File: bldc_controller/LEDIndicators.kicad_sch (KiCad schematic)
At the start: 4 parts

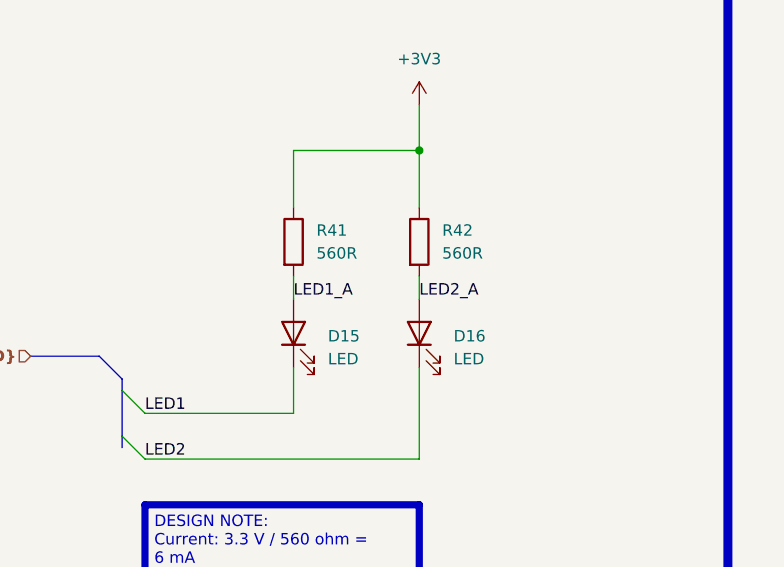
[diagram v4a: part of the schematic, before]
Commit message: routed all signals. TODO: redo all power polygons and ensure good return paths/reference. Added 3d models
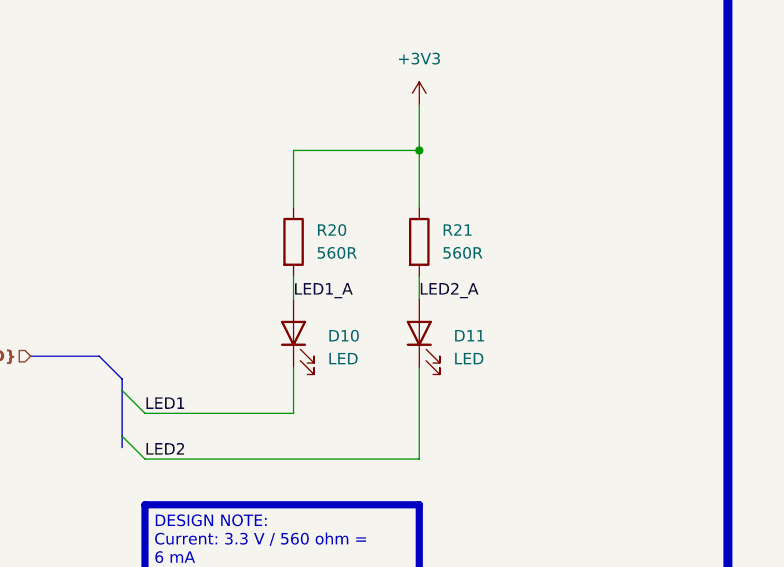
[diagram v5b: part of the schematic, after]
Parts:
- renumbered D15 to D10, D16 to D11, R41 to R20, R42 to R21
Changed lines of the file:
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@@
   (symbol (lib_id "Device:R") (at 162.56 78.74 0) (unit 1)
     (in_bom yes) (on_board yes) (dnp no) (fields_autoplaced)
-    (property "Reference" "R42" (at 165.1 77.47 0)
+    (property "Reference" "R21" (at 165.1 77.47 0)
       (effects (font (size 1.27 1.27)) (justify left))
     )
@@
       (project "bldc_controller"
         (path "/0650c7a8-acba-429c-9f8e-eec0baf0bc1c/fede4c36-00cc-4d3d-b71c-5243ba232202/37954a46-d14f-4062-b94e-09ed11854078"
-          (reference "R42") (unit 1)
+          (reference "R21") (unit 1)
         )
       )
@@
   (symbol (lib_id "Device:R") (at 148.59 78.74 0) (unit 1)
     (in_bom yes) (on_board yes) (dnp no) (fields_autoplaced)
-    (property "Reference" "R41" (at 151.13 77.47 0)
+    (property "Reference" "R20" (at 151.13 77.47 0)
       (effects (font (size 1.27 1.27)) (justify left))
     )
@@
       (project "bldc_controller"
         (path "/0650c7a8-acba-429c-9f8e-eec0baf0bc1c/fede4c36-00cc-4d3d-b71c-5243ba232202/37954a46-d14f-4062-b94e-09ed11854078"
-          (reference "R41") (unit 1)
+          (reference "R20") (unit 1)
         )
       )
@@
   (symbol (lib_id "power:+3V3") (at 162.56 63.5 0) (unit 1)
     (in_bom yes) (on_board yes) (dnp no) (fields_autoplaced)
-    (property "Reference" "#PWR046" (at 162.56 67.31 0)
+    (property "Reference" "#PWR039" (at 162.56 67.31 0)
       (effects (font (size 1.27 1.27)) hide)
     )
@@
       (project "bldc_controller"
         (path "/0650c7a8-acba-429c-9f8e-eec0baf0bc1c/fede4c36-00cc-4d3d-b71c-5243ba232202/37954a46-d14f-4062-b94e-09ed11854078"
-          (reference "#PWR046") (unit 1)
+          (reference "#PWR039") (unit 1)
         )
       )
@@
   (symbol (lib_id "Device:LED") (at 162.56 88.9 90) (unit 1)
     (in_bom yes) (on_board yes) (dnp no) (fields_autoplaced)
-    (property "Reference" "D16" (at 166.37 89.2175 90)
+    (property "Reference" "D11" (at 166.37 89.2175 90)
       (effects (font (size 1.27 1.27)) (justify right))
     )
@@
       (project "bldc_controller"
         (path "/0650c7a8-acba-429c-9f8e-eec0baf0bc1c/fede4c36-00cc-4d3d-b71c-5243ba232202/37954a46-d14f-4062-b94e-09ed11854078"
-          (reference "D16") (unit 1)
+          (reference "D11") (unit 1)
         )
       )
@@
   (symbol (lib_id "Device:LED") (at 148.59 88.9 90) (unit 1)
     (in_bom yes) (on_board yes) (dnp no) (fields_autoplaced)
-    (property "Reference" "D15" (at 152.4 89.2175 90)
+    (property "Reference" "D10" (at 152.4 89.2175 90)
       (effects (font (size 1.27 1.27)) (justify right))
     )
@@
       (project "bldc_controller"
         (path "/0650c7a8-acba-429c-9f8e-eec0baf0bc1c/fede4c36-00cc-4d3d-b71c-5243ba232202/37954a46-d14f-4062-b94e-09ed11854078"
-          (reference "D15") (unit 1)
+          (reference "D10") (unit 1)
         )
       )
